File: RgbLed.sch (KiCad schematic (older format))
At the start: 7 parts, among them Q1 BC817, Q2 BC817, Q3 BC817

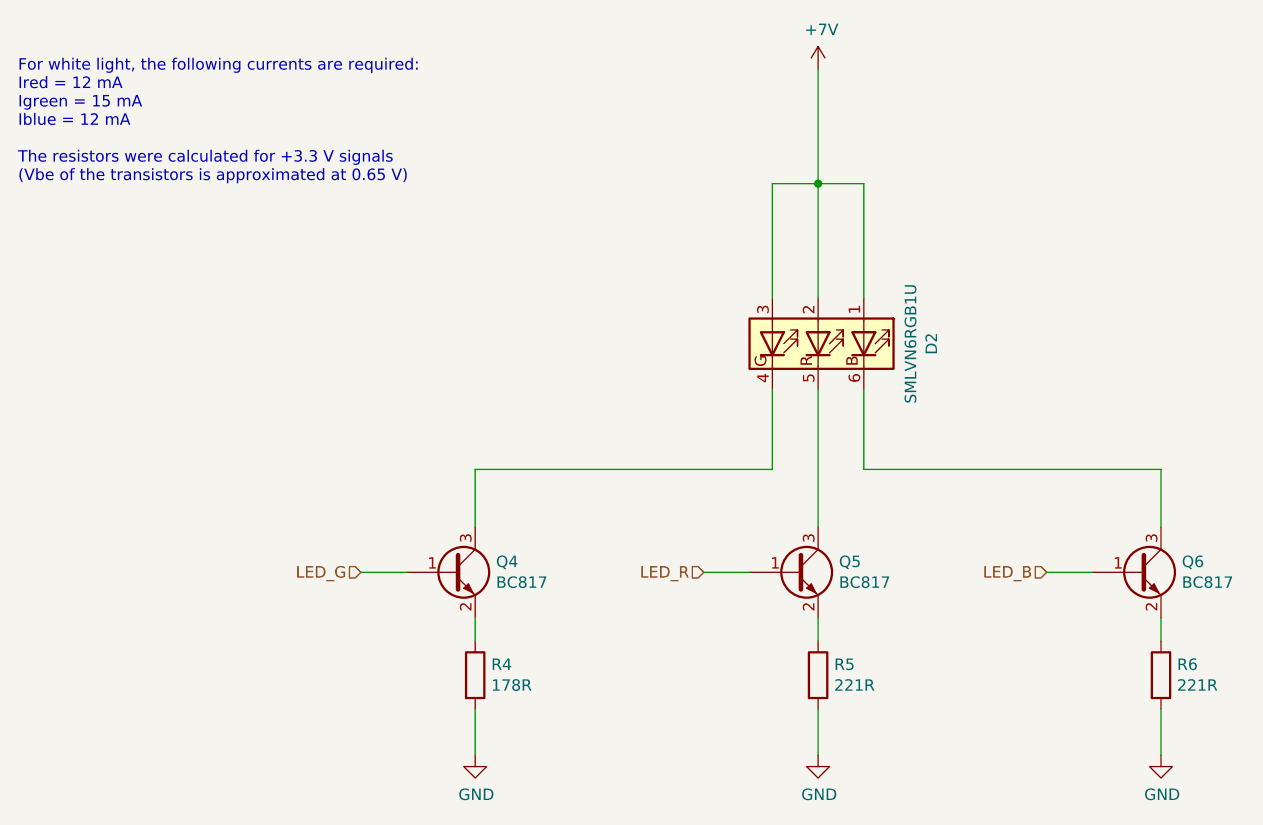
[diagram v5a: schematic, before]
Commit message: Add fuse and more inter-page signals
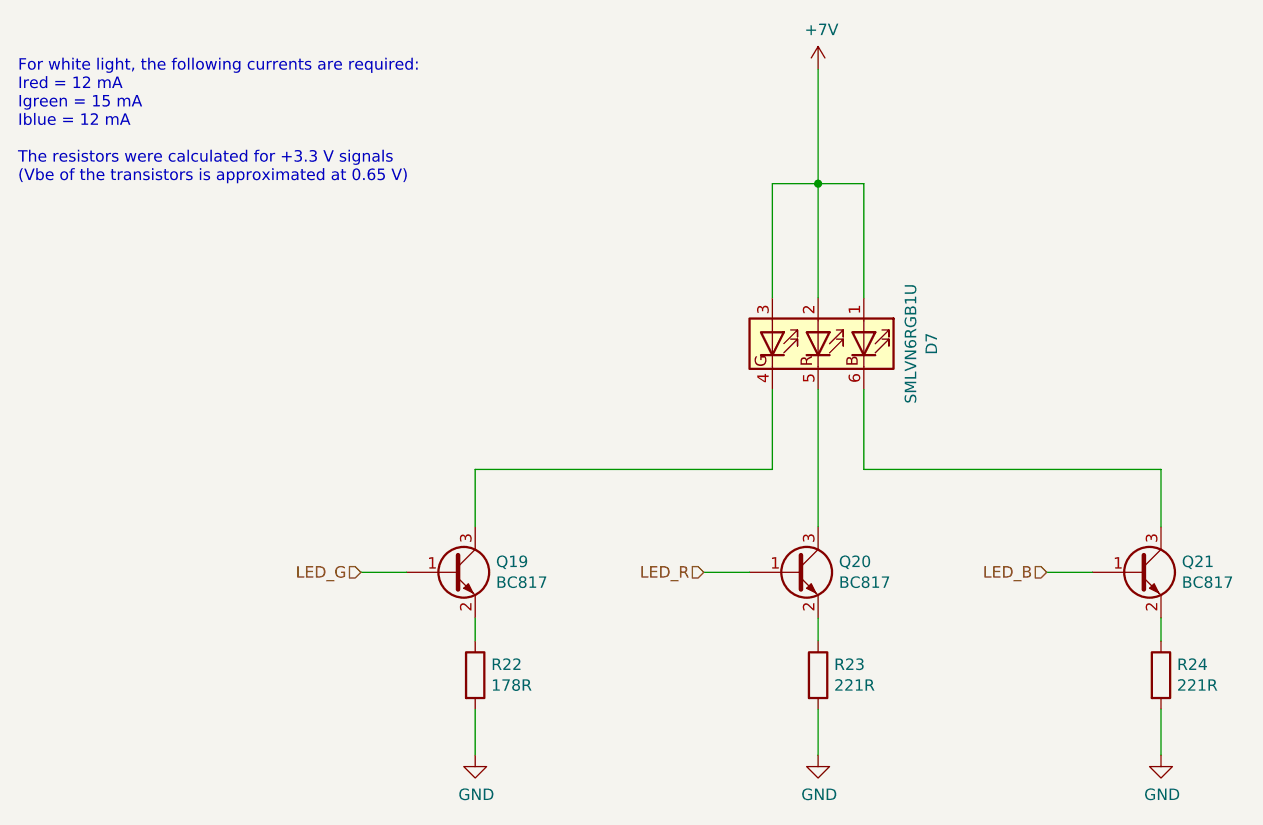
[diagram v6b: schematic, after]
